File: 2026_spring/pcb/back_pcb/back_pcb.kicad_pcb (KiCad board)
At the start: 2 copper layers, 67 x 88.9 mm, 20 parts, among them J1 front joystick, J2 bottom joystick, J3 Arduino, J4 Arduino, SW1 Left Trigger, SW10 Home, SW11 Start, SW13 A, SW14 X, SW15 Y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

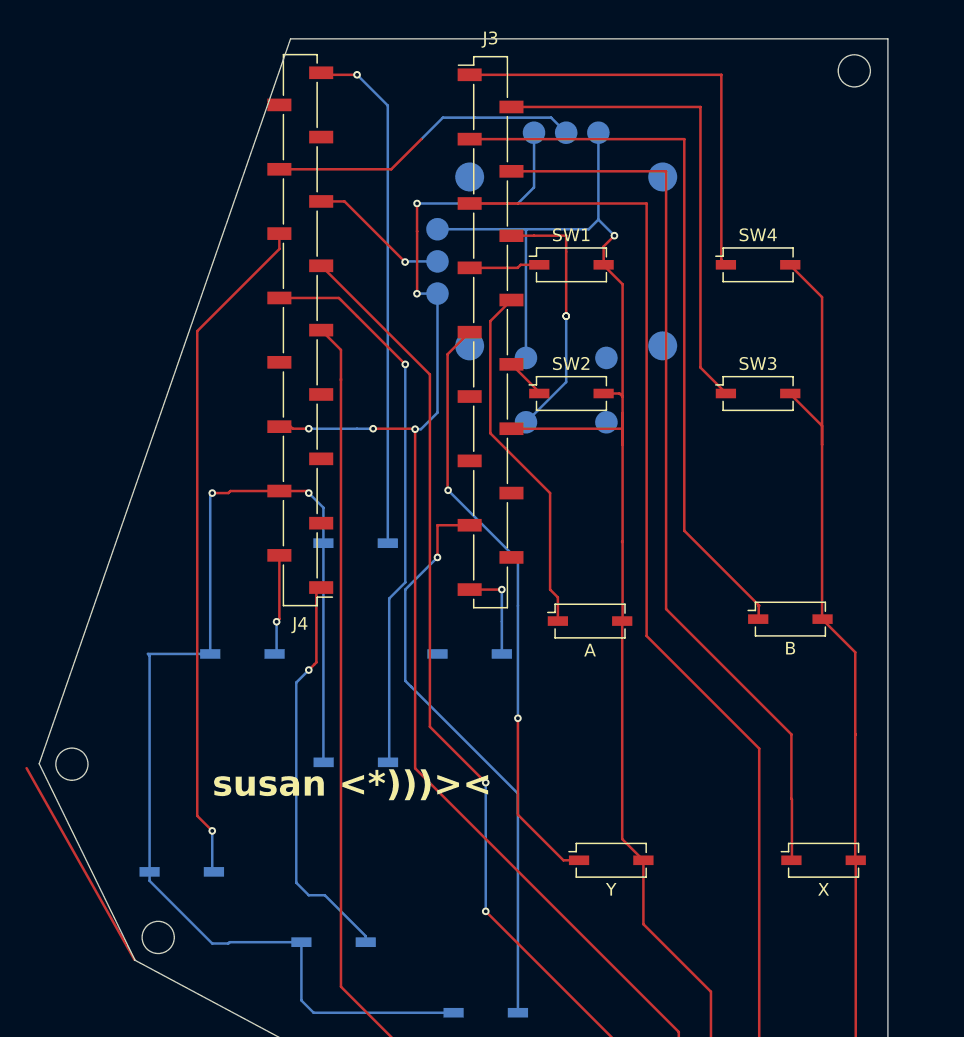
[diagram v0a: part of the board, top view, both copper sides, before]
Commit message: fix back pcb labels
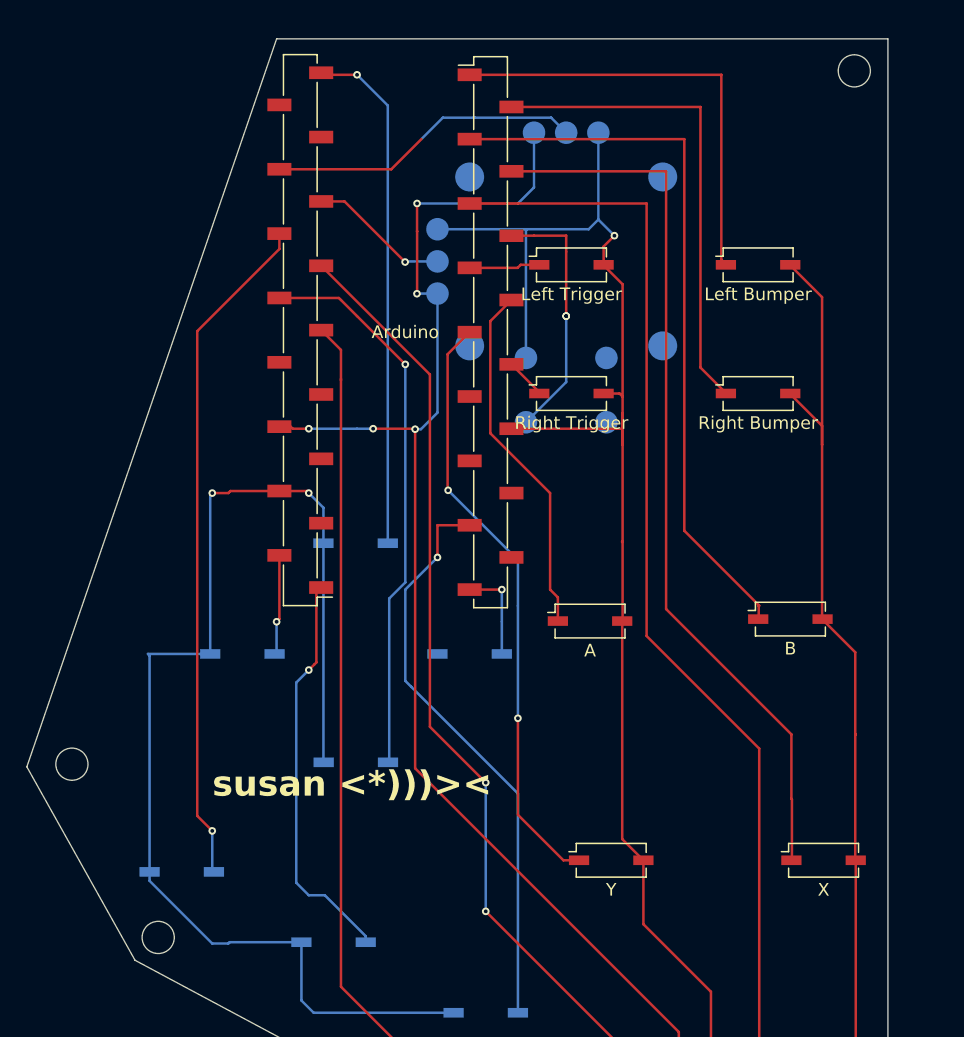
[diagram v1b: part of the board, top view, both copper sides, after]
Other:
- board size 67 x 88.9 mm -> 68 x 88.9 mm
- board text removed: "vyp@mit.edu"
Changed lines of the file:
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@@
 		(property "Reference" "J3"
 			(at 0 -23.19 0)
-			(layer "F.SilkS")
+			(layer "F.Fab")
 			(effects
 				(font
@@
 		(property "Reference" "SW1"
 			(at 0 -2.33 0)
-			(layer "F.SilkS")
+			(layer "F.Fab")
 			(effects
 				(font
@@
 		(property "Value" "Left Trigger"
 			(at 0 2.33 0)
-			(layer "F.Fab")
+			(layer "F.SilkS")
 			(effects
 				(font
@@
 		(property "Reference" "SW2"
 			(at 0 -2.33 0)
-			(layer "F.SilkS")
+			(layer "F.Fab")
 			(effects
 				(font
@@
 		(property "Value" "Right Trigger"
 			(at 0 2.33 0)
-			(layer "F.Fab")
+			(layer "F.SilkS")
 			(effects
 				(font
@@
 		(property "Reference" "SW4"
 			(at 0 -2.33 0)
-			(layer "F.SilkS")
+			(layer "F.Fab")
 			(effects
 				(font
@@
 		(property "Value" "Left Bumper"
 			(at 0 2.33 0)
-			(layer "F.Fab")
+			(layer "F.SilkS")
 			(effects
 				(font
@@
 		(property "Reference" "SW3"
 			(at 0 -2.33 0)
-			(layer "F.SilkS")
+			(layer "F.Fab")
 			(effects
 				(font
@@
 		(property "Value" "Right Bumper"
 			(at 0 2.33 0)
-			(layer "F.Fab")
+			(layer "F.SilkS")
 			(effects
 				(font
@@
 		(property "Reference" "J4"
 			(at 0 -23.19 180)
-			(layer "F.SilkS")
+			(layer "F.Fab")
 			(effects
 				(font
@@
 		)
 		(property "Value" "Arduino"
-			(at 0 23.19 180)
-			(layer "F.Fab")
+			(at -8.291583 -0.161955 180)
+			(layer "F.SilkS")
 			(effects
 				(font
@@
 		(property "Reference" "SW9"
 			(at 0 2.33 180)
-			(layer "B.SilkS")
+			(layer "B.Fab")
 			(effects
 				(font
@@
 		(property "Value" "Left"
 			(at 0 -2.33 180)
-			(layer "B.Fab")
+			(layer "B.SilkS")
 			(effects
 				(font
@@
 		(at 86.36 64.262)
 		(property "Reference" "J1"
-			(at -2.625 15.235 360)
-			(layer "B.SilkS")
+			(at -2.625 15.235 0)
+			(layer "B.Fab")
 			(effects
 				(font
@@
 		)
 		(property "Value" "front joystick"
-			(at 3.09 -14.265 360)
-			(layer "B.Fab")
+			(at 0 -14.265 0)
+			(layer "B.SilkS")
 			(effects
 				(font
@@
 		(property "Reference" "SW8"
 			(at 0 2.33 180)
-			(layer "B.SilkS")
+			(layer "B.Fab")
 			(effects
 				(font
@@
 		(property "Value" "Right"
 			(at 0 -2.33 180)
-			(layer "B.Fab")
+			(layer "B.SilkS")
 			(effects
 				(font
@@
 		(property "Reference" "SW6"
 			(at 0 2.33 180)
-			(layer "B.SilkS")
+			(layer "B.Fab")
 			(effects
 				(font
@@
 		(property "Value" "Down"
 			(at 0 -2.33 180)
-			(layer "B.Fab")
+			(layer "B.SilkS")
 			(effects
 				(font
@@
 	)
 	(gr_line
-		(start 43.762822 104.269)
-		(end 52.284587 119.396394)
-		(stroke
-			(width 0.2)
-			(type default)
-		)
-		(layer "F.Cu")
-	)
-	(gr_line
-		(start 64.6 46.69279)
-		(end 44.757099 103.916044)
+		(start 63.5 46.69279)
+		(end 43.782089 104.162019)
 		(stroke
 			(width 0.05)
@@
 	)
 	(gr_line
-		(start 64.6 46.69279)
+		(start 63.5 46.69279)
 		(end 111.76 46.69279)
 		(stroke
@@
 	)
 	(gr_line
-		(start 44.757099 103.916044)
+		(start 43.782089 104.162019)
 		(end 52.324 119.43279)
 		(stroke
@@
 	)
 	(gr_line
-		(start 43.76 104.14)
-		(end 63.598566 46.687491)
-		(stroke
-			(width 0.1)
-			(type default)
-		)
-		(layer "User.4")
-	)
-	(gr_line
 		(start 86.36 64.262)
 		(end 86.36 51.362)
@@
 		(layer "User.4")
 	)
-	(gr_text "vyp@mit.edu"
-		(at 78.74 50.8 0)
-		(layer "B.SilkS")
-		(effects
-			(font
-				(size 2 2)
-				(thickness 0.4)
-				(bold yes)
-			)
-			(justify right bottom mirror)
-		)
-	)
 	(gr_text "susan <*)))><\n"
